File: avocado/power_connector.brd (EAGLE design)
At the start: 14 x 9 mm, 1 part

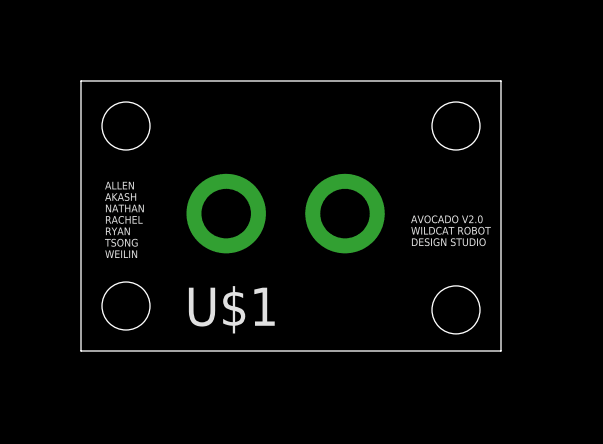
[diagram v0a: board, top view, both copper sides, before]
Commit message: finalized optical encoder and power connector boards
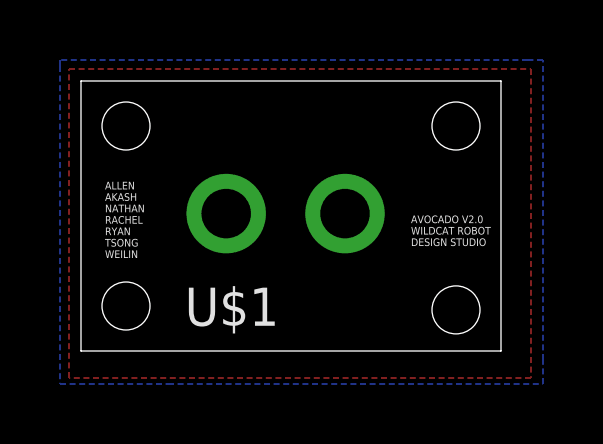
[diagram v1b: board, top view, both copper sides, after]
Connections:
- new net GND: U$1.GND
- new net PWR: U$1.PWR
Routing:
- added copper zone on layer 16, net GND
- added copper zone on layer 1, net PWR
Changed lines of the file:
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@@
 </elements>
 <signals>
+<signal name="PWR">
+<polygon width="0.1524" layer="1" thermals="no">
+<vertex x="-0.4" y="9.4"/>
+<vertex x="15" y="9.4"/>
+<vertex x="15" y="-0.9"/>
+<vertex x="-0.4" y="-0.9"/>
+</polygon>
+<contactref element="U$1" pad="PWR"/>
+</signal>
+<signal name="GND">
+<polygon width="0.1524" layer="16" thermals="no">
+<vertex x="-0.7" y="9.5"/>
+<vertex x="-0.7" y="-1.1"/>
+<vertex x="2.9" y="-1.1"/>
+<vertex x="15.4" y="-1.1"/>
+<vertex x="15.4" y="-0.3"/>
+<vertex x="15.4" y="9.7"/>
+<vertex x="14.9" y="9.7"/>
+<vertex x="-0.7" y="9.7"/>
+</polygon>
+<contactref element="U$1" pad="GND"/>
+</signal>
 </signals>
 </board>
